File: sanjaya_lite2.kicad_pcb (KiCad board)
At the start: 2 copper layers, 110 parts, among them J1 12V_Out, J10 Adap_In, J11 DCDC_Bypass, J12 Conn_RS485, J13 Bat_Bypass+, J14 J_Bat, J15 Conn_420_1, J16 Conn_420_2, J17 Conn_420_3, J18 Conn_420_4, J19 Volt_check_5V, J2 J_SW_Esp, J20 Pwr_SW, J21 J_SW_Sim800, J22 UART_Sim800, J23 Bat_Prot_Bypass, J24 Bat_Bypass-, J3 5V_Out, J4 J_LED, J5 VBat_Out, J6 Conn_I2C, J7 Conn_SPI, J8 Conn_I2C, J9 J_UART_DBG, Q1 PMOS_SI2369DS, Q2 BSS138, Q3 BSS138, SW1 SW_Reset, SW2 SW_Boot, U1 ESP32-WROOM-32, U2 MCP1700-3302E_SOT23, U3 SN65HVD75DR, U5 MCP3428

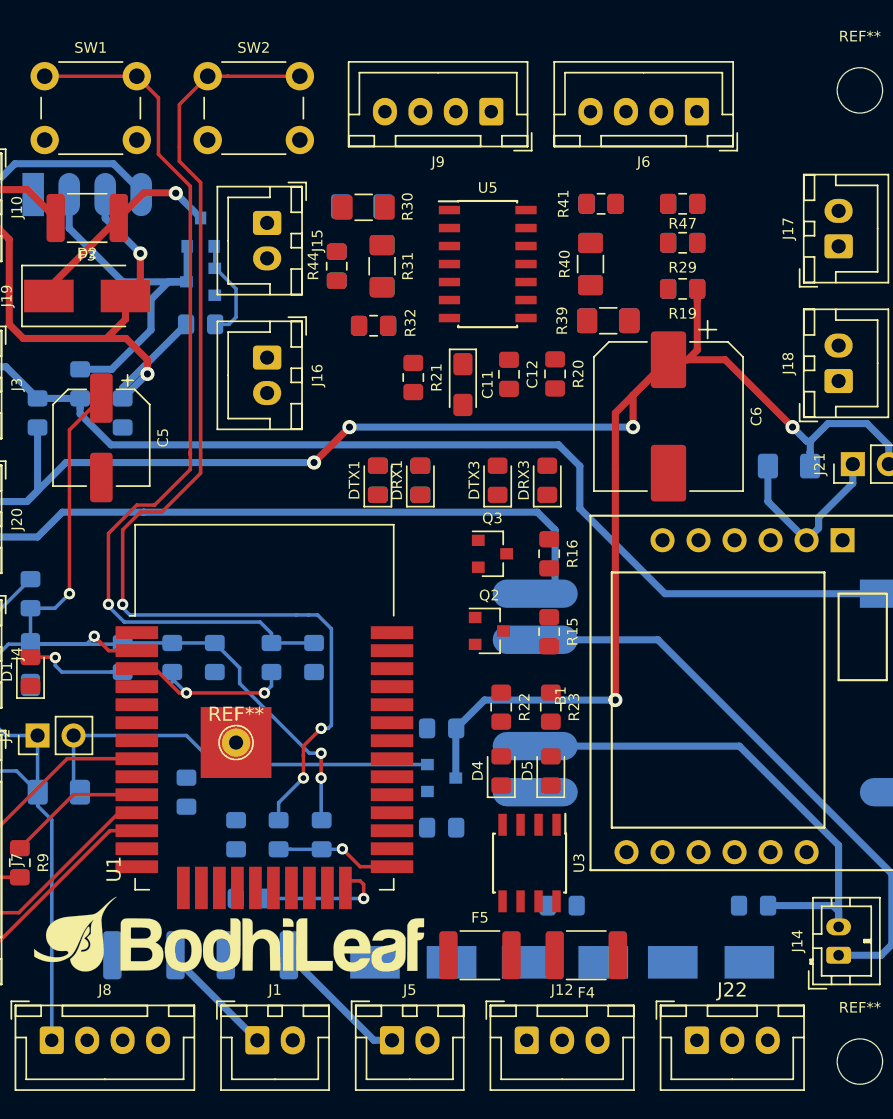
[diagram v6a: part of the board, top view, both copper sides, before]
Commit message: Routing for ESP, Sim800, RS485 done. ADC and terminal routing not yet done.
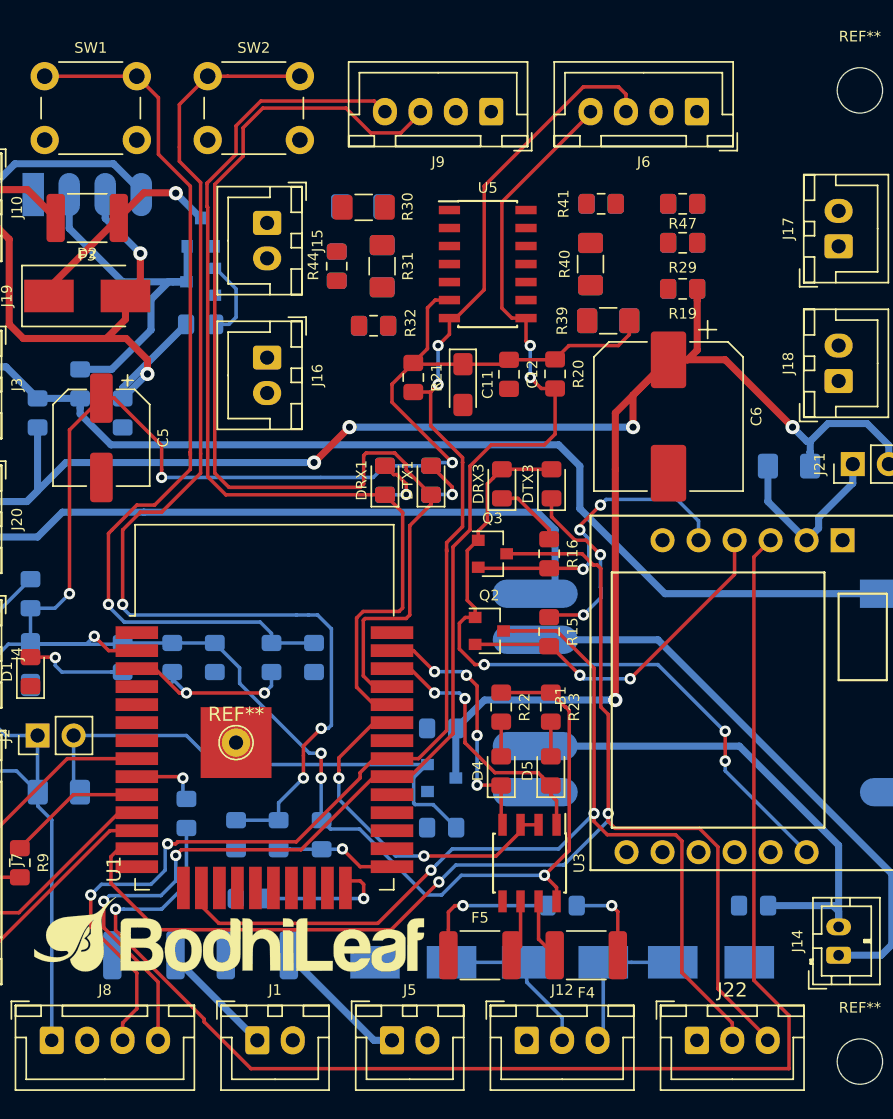
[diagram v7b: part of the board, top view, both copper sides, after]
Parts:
- moved DTX3 3.81 mm to (132.8, 87.8)
- moved DTX1 3.75 mm to (124.2, 87.5)
- moved R10 3.75 mm to (124.2, 87.5)
- moved DRX3 3.21 mm to (129.2, 87.8)
- moved DRX1 2.50 mm to (121.0, 87.5)
- moved R11 2.50 mm to (121.0, 87.5)
- moved R12 1.50 mm to (107.0, 111.0)
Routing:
- net /SCL: track 0.00 -> 102.3 mm, vias 0 -> 4
- net /Sim800_RST: track 0.00 -> 101.6 mm, vias 0 -> 1
- net /Esp_I_Sense+: track 96.7 -> 196.5 mm, vias 4 -> 7
- net /SDA: track 0.00 -> 96.3 mm, vias 0 -> 4
- net Net-(J22-Pad3): track 0.00 -> 93.3 mm, vias 0 -> 2
- net Net-(DTX1-Pad1): track 0.00 -> 77.3 mm
- net Net-(J22-Pad2): track 0.00 -> 73.8 mm, vias 0 -> 2
- net Net-(DRX1-Pad1): track 0.00 -> 69.6 mm
- net Net-(B1-Pad12): track 0.00 -> 50.4 mm, vias 0 -> 3
- net Net-(B1-Pad4): track 0.00 -> 24.8 mm, vias 0 -> 2
- net /rs485/DE: track 0.00 -> 24.1 mm, vias 0 -> 2
- net Net-(B1-Pad5): track 0.00 -> 22.1 mm, vias 0 -> 3
- net /rs485/A: track 0.00 -> 22.1 mm, vias 0 -> 1
- net /rs485/RO: track 0.00 -> 19.9 mm, vias 0 -> 2
- net /rs485/DI: track 0.00 -> 19.1 mm, vias 0 -> 4
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
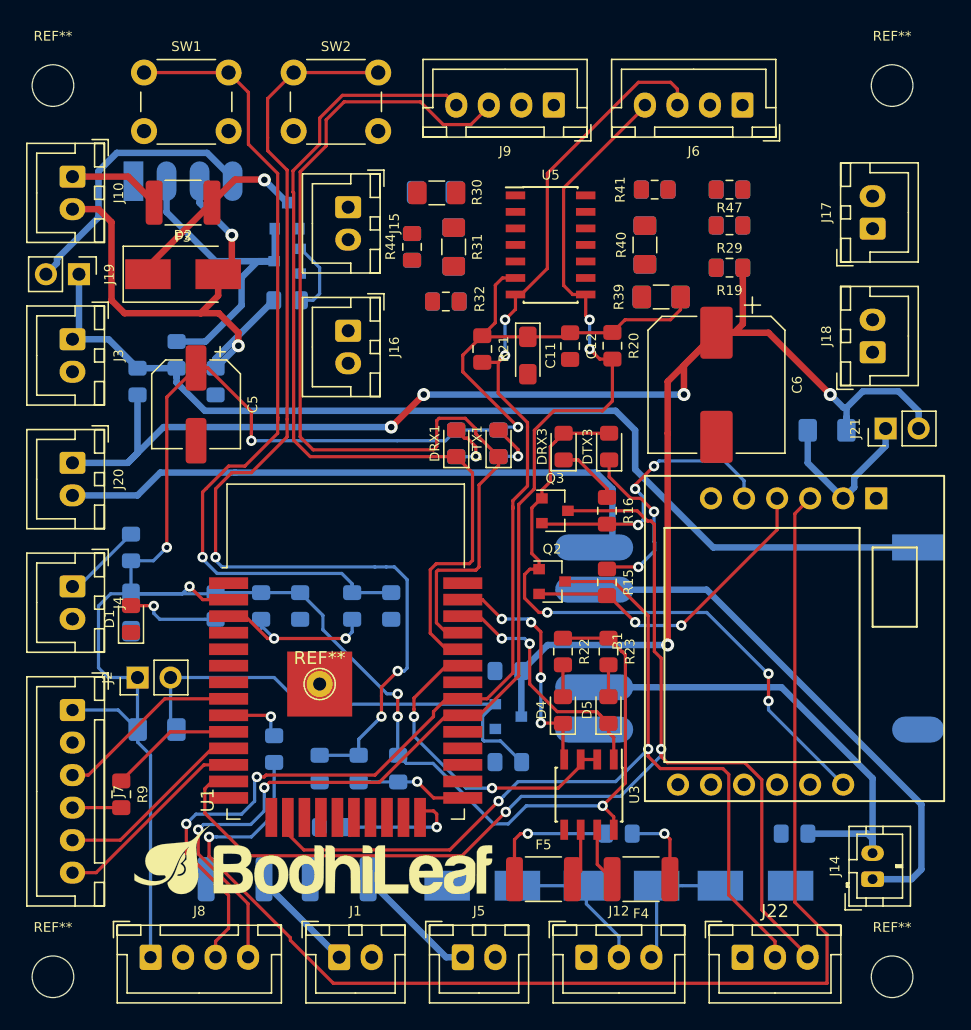
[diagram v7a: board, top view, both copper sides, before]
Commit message: Routing other than ground signal completed
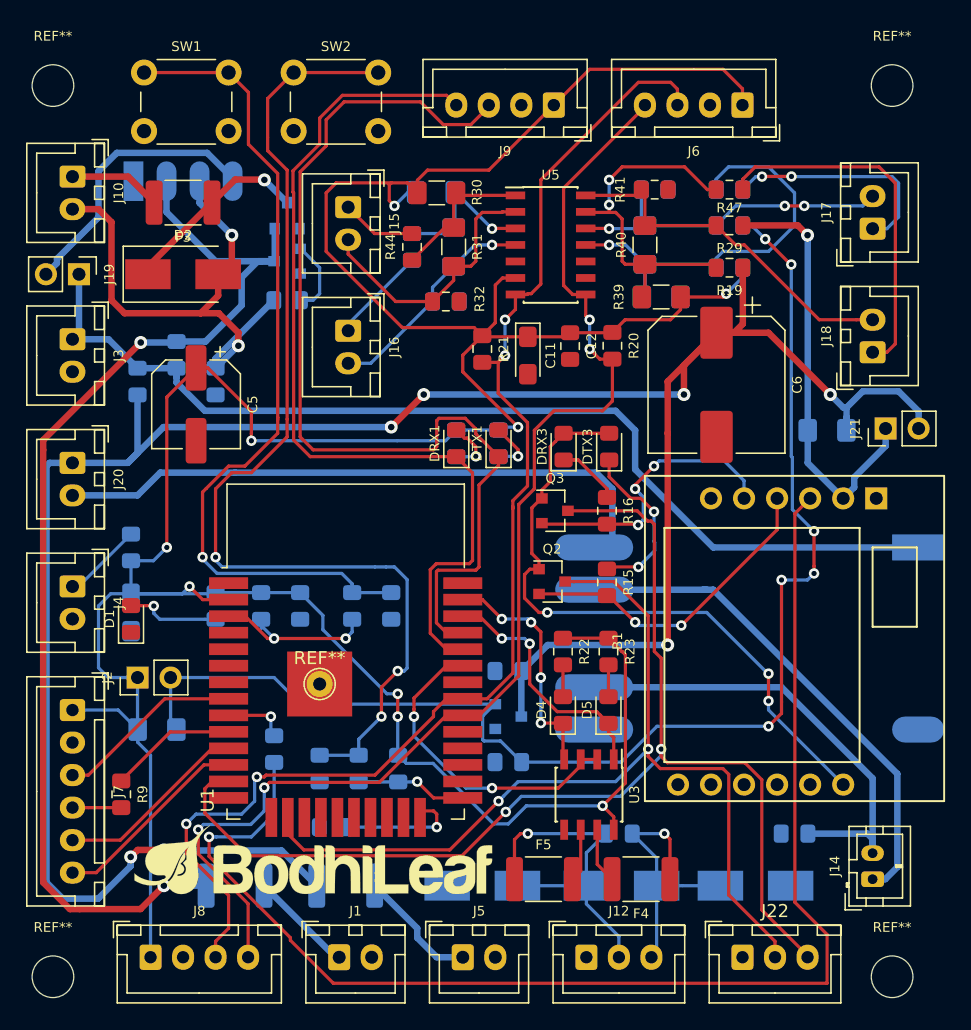
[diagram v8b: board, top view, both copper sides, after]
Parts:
- moved F2 0.71 mm to (112.5, 121.5)
- moved F1 0.50 mm to (104.0, 121.5)
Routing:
- net /Esp_I_Sense+: track 196.5 -> 264.9 mm, vias 7 -> 9
- net /Esp_I_Sense-: track 36.9 -> 100.8 mm, vias 0 -> 6
- net /12V_Out: track 25.3 -> 86.8 mm, vias 0 -> 2
- net /Sim800_I_Sense+: track 130.4 -> 188.9 mm, vias 5 -> 7
- net Net-(R17-Pad1): track 0.00 -> 31.7 mm, vias 0 -> 1
- net Net-(R19-Pad1): track 0.00 -> 28.2 mm, vias 0 -> 2
- net Net-(J18-Pad2): track 0.00 -> 28.0 mm
- net Net-(J18-Pad1): track 0.00 -> 27.8 mm
- net Net-(J17-Pad2): track 0.00 -> 26.0 mm, vias 0 -> 3
- net Net-(J15-Pad2): track 0.00 -> 20.9 mm
- net /Sim800_I_Sense-: track 13.1 -> 33.4 mm, vias 0 -> 1
- net Net-(J17-Pad1): track 0.00 -> 17.6 mm, vias 0 -> 2
- net Net-(J16-Pad2): track 0.00 -> 17.3 mm, vias 0 -> 1
- net Net-(R33-Pad2): track 0.00 -> 12.0 mm, vias 0 -> 1
- net Net-(R30-Pad2): track 0.00 -> 11.6 mm
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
